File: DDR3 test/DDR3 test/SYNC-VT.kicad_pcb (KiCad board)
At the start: 6 copper layers, 65 x 30 mm, 79 parts, among them U1 MPM3834CGPA-Z, U2 MPM3834CGPA-Z, U3 XC7Z010-1CLG225I, U4 TPS3106K33DBVR, U5 W25Q128JVS, U6 0473092651, U7 MT41K256M16TW-107:P, U7 S80KS5123GABHA020, U8 MPM3834CGPA-Z, U8 S80KS5123GABHA020, X1 SIT8008BI-73-XXS-33.333333

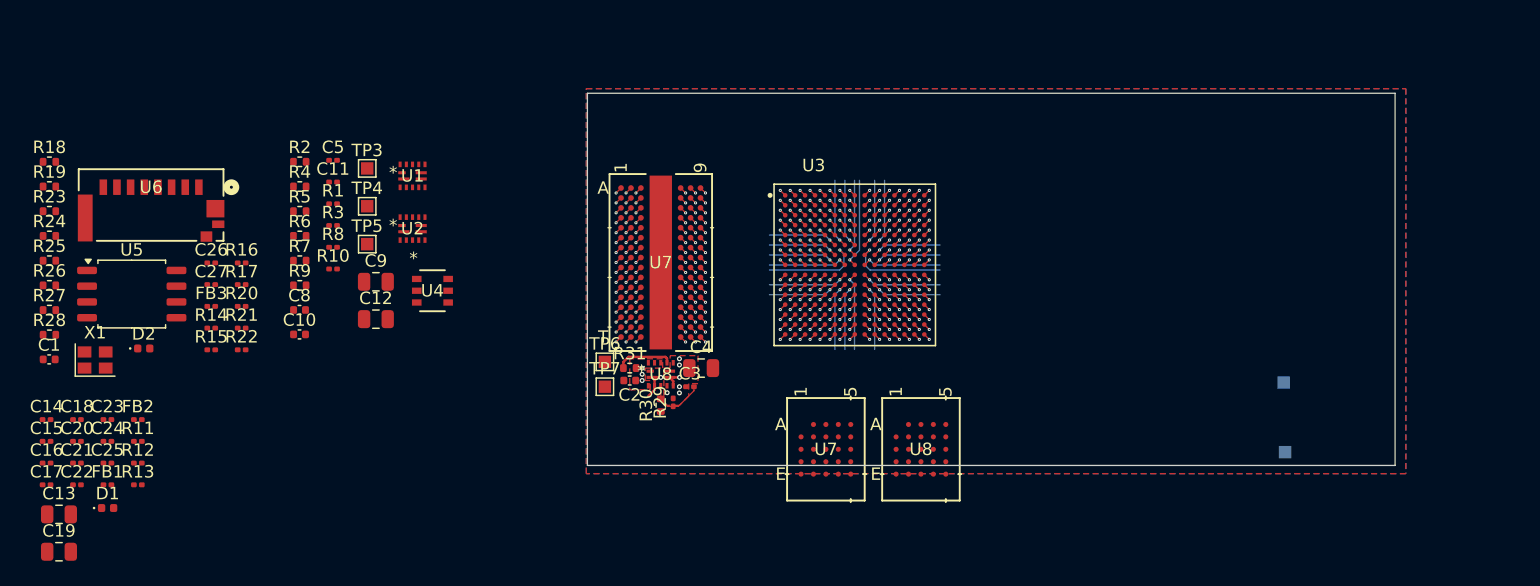
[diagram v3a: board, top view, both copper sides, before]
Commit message: pin assignments
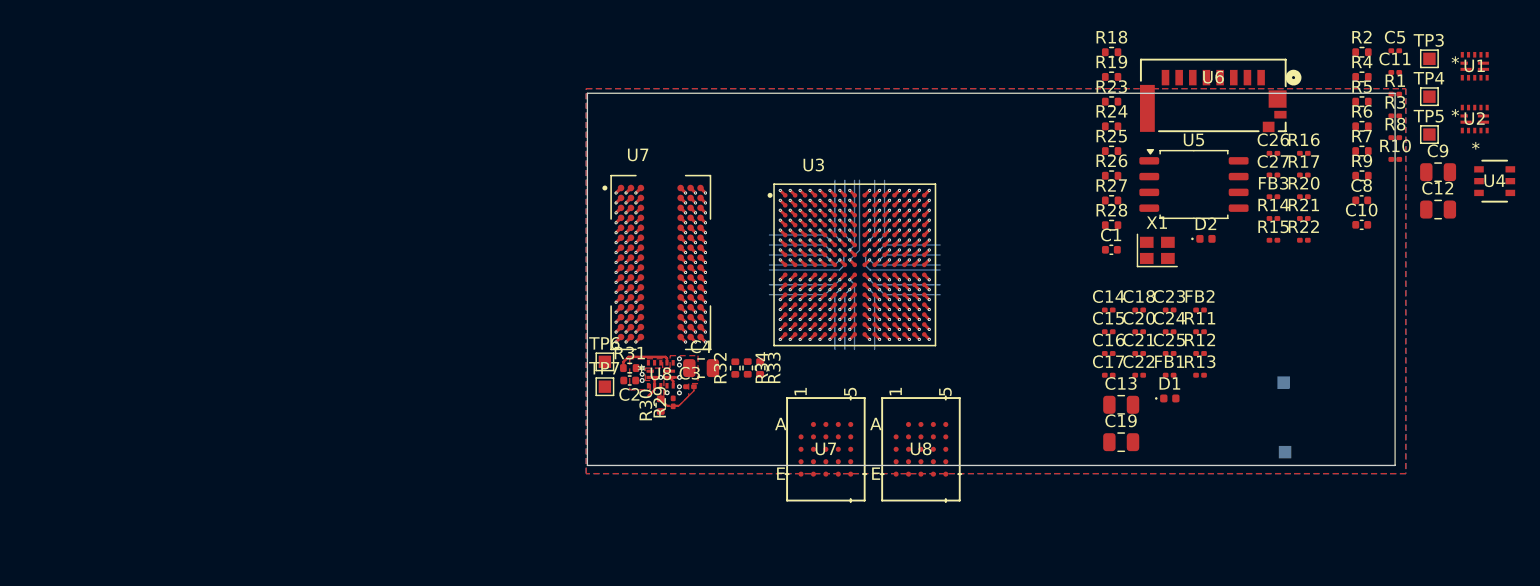
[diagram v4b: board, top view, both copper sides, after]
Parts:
- added R32: 240, Resistor_SMD:R_0402_1005Metric, F.Cu at (91.0, 57.5)
- added R33: 80, Resistor_SMD:R_0402_1005Metric, F.Cu at (93.0, 57.5)
- added R34: 80, Resistor_SMD:R_0402_1005Metric, F.Cu at (92.0, 57.5)
- U7: value MT41K256M16TW-107:P -> MT41K512M16VRP-107_IT_P_TR; footprint Sync_VT extras:FBGA96_8X14_MRN -> Sync_VT extras:IC_MT41K512M16VRP-107_IT_P_TR
- moved C10 86.0 mm to (141.4, 46.0)
- moved C12 86.0 mm to (147.6, 44.7)
- moved C13 86.0 mm to (122.1, 60.5)
- moved C14 86.0 mm to (121.1, 52.8)
- moved C15 86.0 mm to (121.1, 54.6)
- moved C16 86.0 mm to (121.1, 56.3)
- moved C17 86.0 mm to (121.1, 58.1)
- moved C18 86.0 mm to (123.5, 52.8)
- moved C19 86.0 mm to (122.1, 63.5)
- moved C20 86.0 mm to (123.5, 54.6)
- moved C21 86.0 mm to (123.5, 56.3)
- moved C22 86.0 mm to (123.5, 58.1)
- moved C23 86.0 mm to (126.0, 52.8)
- moved C24 86.0 mm to (126.0, 54.6)
- moved C25 86.0 mm to (126.0, 56.3)
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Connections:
- net /RAM/DDR4_A0 renamed /RAM/DDR_A0
- net /RAM/DDR4_A1 renamed /RAM/DDR_A1
- net /RAM/DDR4_A10 renamed /RAM/DDR_A10
- net /RAM/DDR4_A11 renamed /RAM/DDR_A11
- net /RAM/DDR4_A12 renamed /RAM/DDR_A12
- net /RAM/DDR4_A13 renamed /RAM/DDR_A13
- net /RAM/DDR4_A14 renamed /RAM/DDR_A14
- net /RAM/DDR4_A2 renamed /RAM/DDR_A2
- net /RAM/DDR4_A3 renamed /RAM/DDR_A3
- net /RAM/DDR4_A4 renamed /RAM/DDR_A4
- net /RAM/DDR4_A5 renamed /RAM/DDR_A5
- net /RAM/DDR4_A6 renamed /RAM/DDR_A6
- net /RAM/DDR4_A7 renamed /RAM/DDR_A7
- net /RAM/DDR4_A8 renamed /RAM/DDR_A8
- net /RAM/DDR4_A9 renamed /RAM/DDR_A9
- net /RAM/DDR4_DQ0 renamed /RAM/DDR_DQ0
- net /RAM/DDR4_DQ1 renamed /RAM/DDR_DQ1
- net /RAM/DDR4_DQ10 renamed /RAM/DDR_DQ10
- net /RAM/DDR4_DQ11 renamed /RAM/DDR_DQ11
- net /RAM/DDR4_DQ12 renamed /RAM/DDR_QD12
- net /RAM/DDR4_DQ13 renamed /RAM/DDR_DQ13
- net /RAM/DDR4_DQ14 renamed /RAM/DDR_DQ14
- net /RAM/DDR4_DQ15 renamed /RAM/DDR_DQ15
- net /RAM/DDR4_DQ2 renamed /RAM/DDR_DQ2
- net /RAM/DDR4_DQ3 renamed /RAM/DDR_DQ3
- net /RAM/DDR4_DQ4 renamed /RAM/DDR_DQ4
- net /RAM/DDR4_DQ5 renamed /RAM/DDR_DQ5
- net /RAM/DDR4_DQ6 renamed /RAM/DDR_DQ6
- net /RAM/DDR4_DQ7 renamed /RAM/DDR_DQ7
- net /RAM/DDR4_DQ8 renamed /RAM/DDR_DQ8
- net /RAM/DDR4_DQ9 renamed /RAM/DDR_DQ9
- U3 pad B1: unconnected-(U3E-PS_DDR_DM0_502-PadB1) -> /RAM/LDM
- U3 pad B2: unconnected-(U3E-PS_DDR_DQS_N0_502-PadB2) -> /RAM/~{LDQS}
- U3 pad C2: unconnected-(U3E-PS_DDR_DQS_P0_502-PadC2) -> /RAM/LDQS
- U3 pad D3: unconnected-(U3E-PS_DDR_DM1_502-PadD3) -> /RAM/UDM
- U3 pad F2: unconnected-(U3E-PS_DDR_DQS_N1_502-PadF2) -> /RAM/~{UDQS}
- U3 pad F4: unconnected-(U3E-PS_DDR_VREF0_502-PadF4) -> /RAM/DDR_VREF
- U3 pad G2: unconnected-(U3E-PS_DDR_DQS_P1_502-PadG2) -> /RAM/UDQS
- U3 pad H3: unconnected-(U3E-PS_DDR_VRP_502-PadH3) -> Net-(U3E-PS_DDR_VRP_502)
- U3 pad J3: unconnected-(U3E-PS_DDR_VRN_502-PadJ3) -> Net-(U3E-PS_DDR_VRN_502)
- U3 pad K3: unconnected-(U3E-PS_DDR_ODT_502-PadK3) -> /RAM/ODT
- U3 pad L3: unconnected-(U3E-PS_DDR_CKE_502-PadL3) -> /RAM/CKE
- U3 pad L4: unconnected-(U3E-PS_DDR_DRST_B_502-PadL4) -> /RAM/~{RESET}
- U3 pad M6: unconnected-(U3E-PS_DDR_BA0_502-PadM6) -> /RAM/DDR_BA0
- U3 pad N2: unconnected-(U3E-PS_DDR_CKN_502-PadN2) -> /RAM/~{CK}
- U3 pad N3: unconnected-(U3E-PS_DDR_CKP_502-PadN3) -> /RAM/CK
- U3 pad N6: unconnected-(U3E-PS_DDR_BA2_502-PadN6) -> /RAM/DDR_BA2
- U3 pad R1: unconnected-(U3E-PS_DDR_BA1_502-PadR1) -> /RAM/DDR_BA1
- U3 pad R2: unconnected-(U3E-PS_DDR_CS_B_502-PadR2) -> /RAM/~{CS}
- U3 pad R3: unconnected-(U3E-PS_DDR_WE_B_502-PadR3) -> /RAM/~{WE}
- U3 pad R5: unconnected-(U3E-PS_DDR_CAS_B_502-PadR5) -> /RAM/~{CAS}
- U3 pad R6: unconnected-(U3E-PS_DDR_RAS_B_502-PadR6) -> /RAM/~{RAS}
- U7 pad A1: unconnected-(U7-VDDQ-PadA1) -> +1V5
- U7 pad A8: unconnected-(U7-VDDQ-PadA8) -> +1V5
- U7 pad A9: unconnected-(U7-VSS-PadA9) -> GND
- U7 pad B1: unconnected-(U7-VSSQ-PadB1) -> GND
- U7 pad B2: unconnected-(U7-VDD-PadB2) -> +1V5
- U7 pad B3: unconnected-(U7-VSS-PadB3) -> GND
- U7 pad B7: unconnected-(U7-*UDQS-PadB7) -> /RAM/~{UDQS}
- U7 pad B9: unconnected-(U7-VSSQ-PadB9) -> GND
- U7 pad C1: unconnected-(U7-VDDQ-PadC1) -> +1V5
- U7 pad C7: unconnected-(U7-UDQS-PadC7) -> /RAM/UDQS
- U7 pad C9: unconnected-(U7-VDDQ-PadC9) -> +1V5
- U7 pad D1: unconnected-(U7-VSSQ-PadD1) -> GND
- U7 pad D2: unconnected-(U7-VDDQ-PadD2) -> +1V5
- U7 pad D3: unconnected-(U7-UDM-PadD3) -> /RAM/UDM
- U7 pad D8: unconnected-(U7-VSSQ-PadD8) -> GND
- U7 pad D9: unconnected-(U7-VDD-PadD9) -> +1V5
- U7 pad E1: unconnected-(U7-VSS-PadE1) -> GND
- U7 pad E2: unconnected-(U7-VSSQ-PadE2) -> GND
- U7 pad E7: unconnected-(U7-LDM-PadE7) -> /RAM/LDM
- U7 pad E8: unconnected-(U7-VSSQ-PadE8) -> GND
- U7 pad E9: unconnected-(U7-VDDQ-PadE9) -> +1V5
- U7 pad F1: unconnected-(U7-VDDQ-PadF1) -> +1V5
- U7 pad F3: unconnected-(U7-LDQS-PadF3) -> /RAM/LDQS
- U7 pad F9: unconnected-(U7-VSSQ-PadF9) -> GND
- U7 pad G1: unconnected-(U7-VSSQ-PadG1) -> GND
- U7 pad G3: unconnected-(U7-*LDQS-PadG3) -> /RAM/~{LDQS}
- U7 pad G7: unconnected-(U7-VDD-PadG7) -> +1V5
- U7 pad G8: unconnected-(U7-VSS-PadG8) -> GND
- U7 pad G9: unconnected-(U7-VSSQ-PadG9) -> GND
- U7 pad H1: unconnected-(U7-VREFDQ-PadH1) -> /RAM/DDR_VREF
- U7 pad H2: unconnected-(U7-VDDQ-PadH2) -> +1V5
- U7 pad H9: unconnected-(U7-VDDQ-PadH9) -> +1V5
- U7 pad J2: unconnected-(U7-VSS-PadJ2) -> GND
- U7 pad J3: unconnected-(U7-*RAS-PadJ3) -> /RAM/~{RAS}
- U7 pad J7: unconnected-(U7-CK-PadJ7) -> /RAM/CK
- U7 pad J8: unconnected-(U7-VSS-PadJ8) -> GND
- U7 pad K1: unconnected-(U7-ODT-PadK1) -> /RAM/ODT
- U7 pad K2: unconnected-(U7-VDD-PadK2) -> +1V5
- U7 pad K3: unconnected-(U7-*CAS-PadK3) -> /RAM/~{CAS}
- U7 pad K7: unconnected-(U7-*CK-PadK7) -> /RAM/~{CK}
- U7 pad K8: unconnected-(U7-VDD-PadK8) -> +1V5
- U7 pad K9: unconnected-(U7-CKE-PadK9) -> /RAM/CKE
- U7 pad L2: unconnected-(U7-*CS-PadL2) -> /RAM/~{CS}
- U7 pad L3: unconnected-(U7-*WE-PadL3) -> /RAM/~{WE}
- U7 pad L8: unconnected-(U7-ZQ-PadL8) -> Net-(U7-ZQ)
- U7 pad M1: unconnected-(U7-VSS-PadM1) -> GND
- U7 pad M2: unconnected-(U7-BA0-PadM2) -> /RAM/DDR_BA0
- U7 pad M3: unconnected-(U7-BA2-PadM3) -> /RAM/DDR_BA2
- U7 pad M7: unconnected-(U7-NC-PadM7) -> GND
- U7 pad M8: unconnected-(U7-VREFCA-PadM8) -> /RAM/DDR_VREF
- U7 pad M9: unconnected-(U7-VSS-PadM9) -> GND
- U7 pad N1: unconnected-(U7-VDD-PadN1) -> +1V5
- U7 pad N8: unconnected-(U7-BA1-PadN8) -> /RAM/DDR_BA1
- U7 pad N9: unconnected-(U7-VDD-PadN9) -> +1V5
- U7 pad P1: unconnected-(U7-VSS-PadP1) -> GND
- U7 pad P9: unconnected-(U7-VSS-PadP9) -> GND
- U7 pad R1: unconnected-(U7-VDD-PadR1) -> +1V5
- U7 pad R9: unconnected-(U7-VDD-PadR9) -> +1V5
- U7 pad T1: unconnected-(U7-VSS-PadT1) -> GND
- U7 pad T2: unconnected-(U7-*RESET-PadT2) -> /RAM/~{RESET}
- U7 pad T9: unconnected-(U7-VSS-PadT9) -> GND
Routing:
- net GND: track 124.9 -> 137.4 mm, vias 34 -> 56
- net +1V5: track 0.00 -> 10.2 mm, vias 5 -> 23
- net /RAM/DDR_VREF: track 0.00 -> 5.13 mm, vias 0 -> 3
- net /RAM/~{RESET}: track 0.00 -> 4.57 mm, vias 0 -> 2
- net /RAM/DDR_BA0: track 0.00 -> 4.51 mm, vias 0 -> 2
- net unconnected-(U3E-PS_DDR_VREF0_502-PadF4): track 4.00 -> 0.00 mm, vias 1 -> 0
- net unconnected-(U3E-PS_DDR_DRST_B_502-PadL4): track 4.00 -> 0.00 mm, vias 1 -> 0
- net unconnected-(U3E-PS_DDR_BA0_502-PadM6): track 3.94 -> 0.00 mm, vias 1 -> 0
- net /RAM/CK: track 0.00 -> 3.77 mm, vias 0 -> 2
- net /RAM/UDM: track 0.00 -> 3.77 mm, vias 0 -> 2
- net /RAM/ODT: track 0.00 -> 3.77 mm, vias 0 -> 2
- net /RAM/CKE: track 0.00 -> 3.77 mm, vias 0 -> 2
- net /RAM/DDR_BA2: track 0.00 -> 3.71 mm, vias 0 -> 2
- net unconnected-(U3E-PS_DDR_CKP_502-PadN3): track 3.21 -> 0.00 mm, vias 1 -> 0
- net unconnected-(U3E-PS_DDR_ODT_502-PadK3): track 3.20 -> 0.00 mm, vias 1 -> 0
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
